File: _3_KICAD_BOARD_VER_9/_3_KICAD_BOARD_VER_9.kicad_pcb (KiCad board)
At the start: 4 copper layers, 85 x 87 mm, 60 parts, among them J1 HTEC8-160-01-X-DV-A-BL-X, J2 PH2-20-UA, J3 PH2-20-UA, J4 PH2-20-UA, J5 PH2-20-UA, J6 PH2-20-UA, U1 AZ1117H-3.3TRE1, U2 dsPIC33AK512MPS505T-I/PT, U3 DAC7564ICPW, U4 FM24W256G, Y1 ABMM-25.000MHZ-B2-T

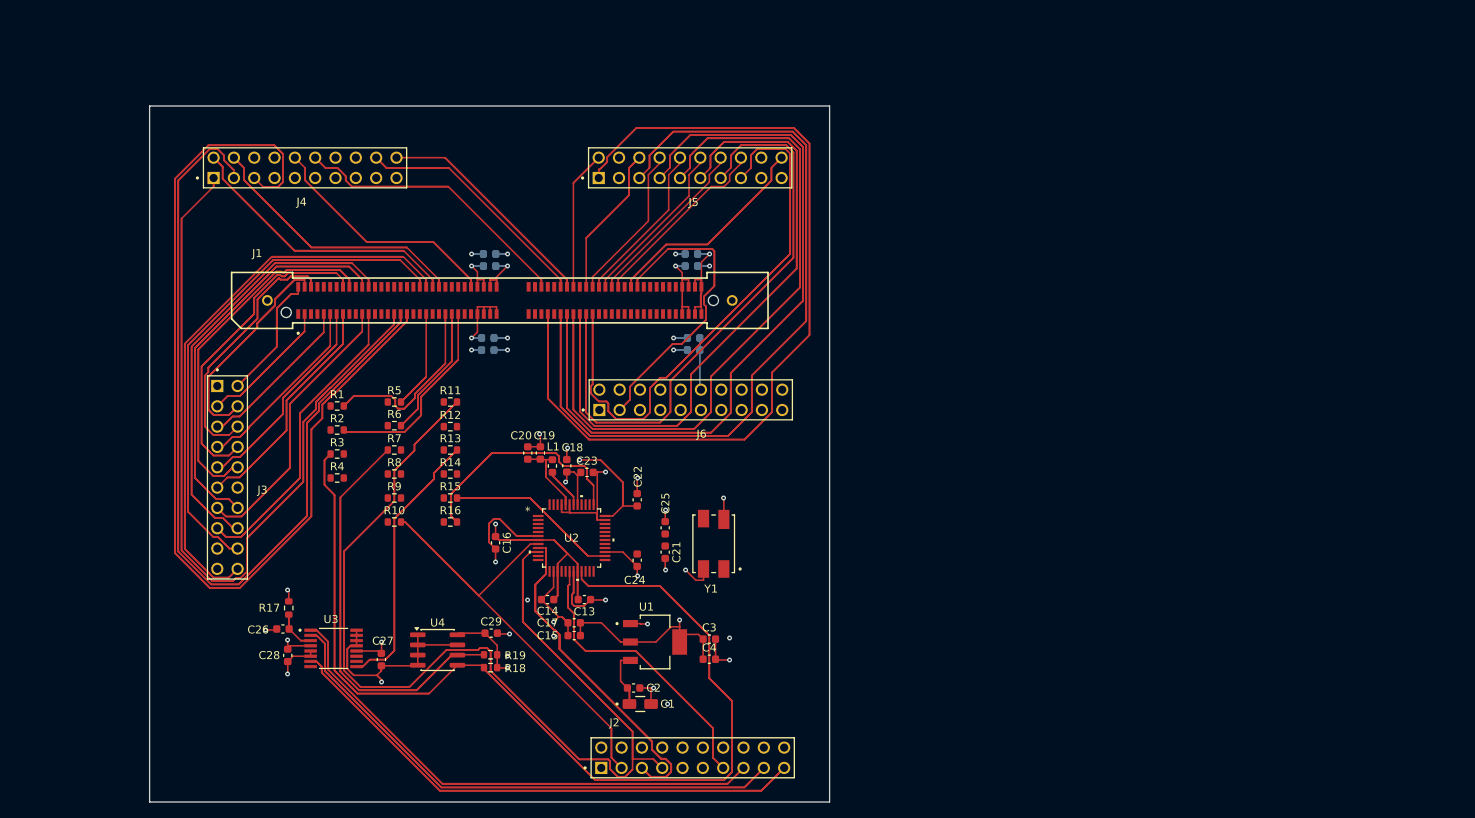
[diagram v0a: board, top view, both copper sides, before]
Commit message: feat : vdd, gnd, vin routing done
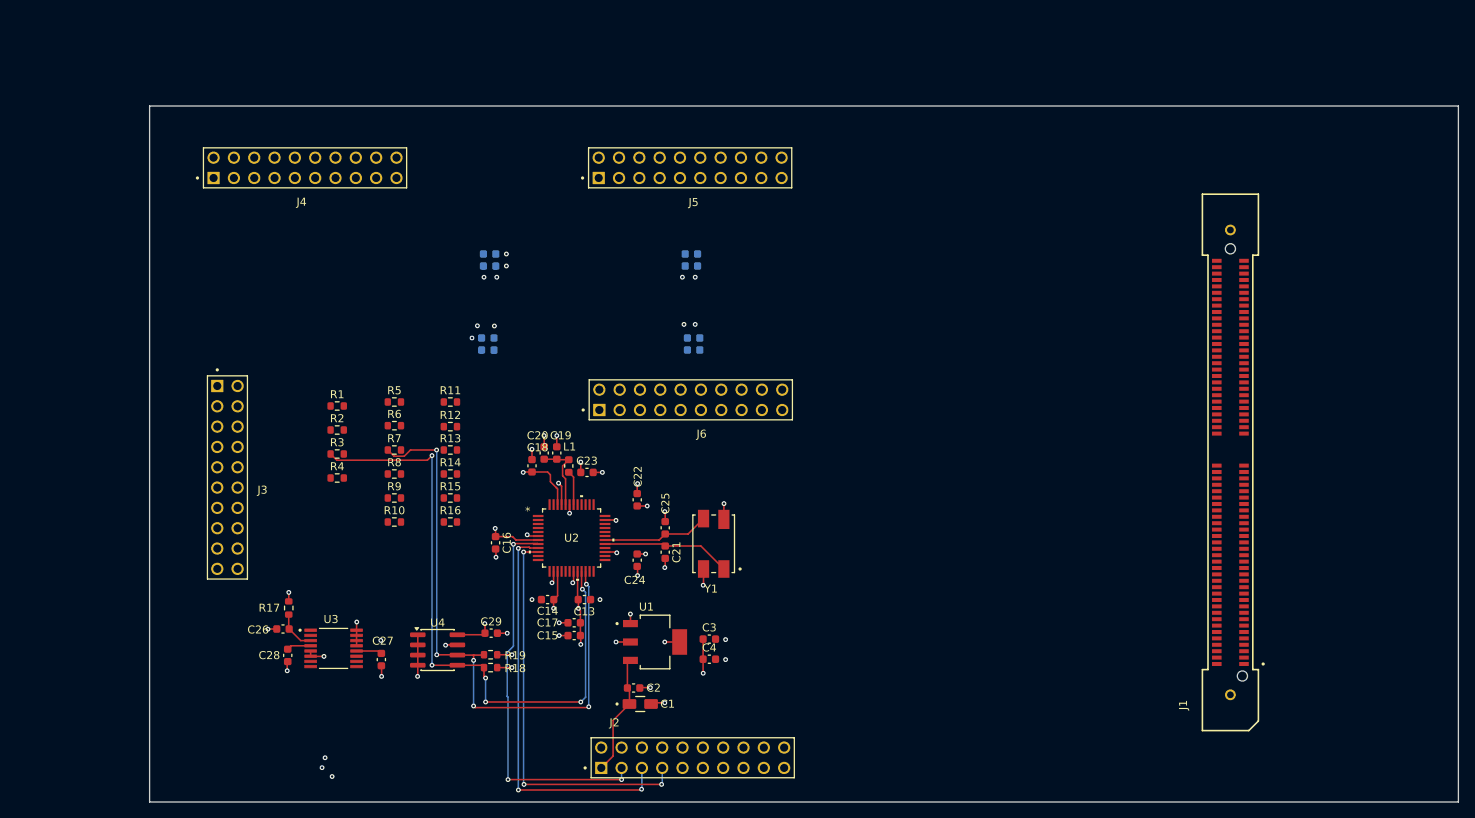
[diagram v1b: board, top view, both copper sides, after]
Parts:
- moved J1 93.5 mm to (220.1, 97.5), turned to 90 degrees
- moved C18 4.35 mm to (132.8, 98.0)
- moved C19 2.05 mm to (135.9, 96.4)
- moved L1 2.05 mm to (137.4, 98.0)
- moved C20 2.05 mm to (134.3, 96.4)
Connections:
- J1 pad 61: +3.3V -> GND
- J1 pad 63: +3.3V -> GND
- J2 pad 14: unconnected-(J2-Pad14) -> /DIM_SHEET/DEBUG_BUS.MCLR
- J2 pad 16: unconnected-(J2-Pad16) -> +3.3V
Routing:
- net /DIM_SHEET/DIM_BUS.IO24: track 244.8 -> 0.00 mm
- net /DIM_SHEET/DIM_BUS.IO22: track 216.8 -> 0.00 mm
- net /DIM_SHEET/DIM_BUS.IO40: track 215.6 -> 0.00 mm
- net /DIM_SHEET/DIM_BUS.IO44: track 196.8 -> 0.00 mm
- net /DIM_SHEET/ADC_BUS._A2: track 246.4 -> 50.3 mm, vias 0 -> 3
- net /DIM_SHEET/DIM_BUS.IO20: track 191.0 -> 0.00 mm
- net /DIM_SHEET/DIM_BUS.IO46: track 184.6 -> 0.00 mm
- net /DIM_SHEET/DIM_BUS.IO48: track 172.3 -> 0.00 mm
- net /DIM_SHEET/I2C_BUS.SDA: track 240.6 -> 79.1 mm, vias 0 -> 6
- net /DIM_SHEET/DIM_BUS.IO50: track 160.1 -> 0.00 mm
- net /DIM_SHEET/DIM_BUS.IO52: track 147.8 -> 0.00 mm
- net /DIM_SHEET/DIM_BUS.IO19: track 137.9 -> 0.00 mm
- net /DIM_SHEET/DIM_BUS.IO54: track 135.4 -> 0.00 mm
- net /SIGNAL_IO_SHEET/DAC_BUS._1: track 134.3 -> 0.00 mm, vias 0 -> 1
- net /SIGNAL_IO_SHEET/DAC_BUS._2: track 134.2 -> 0.00 mm, vias 0 -> 1
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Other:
- board size 85 x 87 mm -> 163.6 x 87 mm

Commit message: feat : dim only project done
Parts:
- removed C22, C23, C24, C26, C27, C28, C29: 100nF, Capacitor_SMD:C_0603_1608Metric
- removed C25: 18pF, Capacitor_SMD:C_0603_1608Metric
- removed J2, J3, J4, J5, J6: PH2-20-UA, PH2-20-UA:ADAM_PH2-20-UA
- removed R10, R11, R12, R13, R14, R15, R16, R4, R5, R6, R7, R8, R9: 0R, Resistor_SMD:R_0603_1608Metric
- removed R17: 100R, Resistor_SMD:R_0603_1608Metric
- removed R18, R19: 2.2K, Resistor_SMD:R_0603_1608Metric
- C10, C6: moved to F.Cu
- C11: value 100nF -> 10uF; moved to F.Cu
- C12, C5, C8: value 22uF -> 100nF; moved to F.Cu
- C13: value 100nF -> 18pF
- C15: value 47uF -> 100nF
- C17: value 1uF -> 18pF
- C19: value 10uF -> 100nF
- C21: value 18pF -> 100nF
- C7: value 100nF -> 47uF; moved to F.Cu
- C9: value 22uF -> 1uF; moved to F.Cu
- J1: value HTEC8-160-01-X-DV-A-BL-X -> PH2-20-UA; footprint HTEC8-160-01-X-DV-A-BL-X:SAMTEC_HTEC8-160-01-X-DV-A-BL-X -> PH2-20-UA:ADAM_PH2-20-UA
- R1: value 0R -> 100R
- R2, R3: value 0R -> 2.2K
- moved J1 124.5 mm to (102.5, 57.0), turned to 0 degrees
- moved C15 68.4 mm to (98.3, 63.5), turned to 0 degrees
- moved C2 65.1 mm to (126.3, 63.5)
- moved C17 63.2 mm to (98.3, 68.5), turned to 0 degrees
- moved C21 62.9 mm to (90.3, 87.3), turned to 0 degrees
- moved C13 62.7 mm to (94.3, 71.0)
- moved C1 62.6 mm to (117.6, 72.1)
- moved C9 62.4 mm to (90.3, 73.5)
- moved C11 61.2 mm to (94.3, 66.0)
- moved C3 60.8 mm to (126.3, 66.0)
- moved C4 60.8 mm to (126.3, 68.5)
- moved U1 60.8 mm to (119.5, 66.4)
- moved C12 60.2 mm to (94.3, 68.5)
- moved C10 59.0 mm to (94.3, 63.5)
- moved Y1 58.7 mm to (104.3, 79.0), turned to 0 degrees
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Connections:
- net /DIM_SHEET/SPI_BUS.MOSI renamed /MCU_48PIN_SHEET/SPI_BUS.MOSI
- net /DIM_SHEET/SPI_BUS.SCLK renamed /MCU_48PIN_SHEET/SPI_BUS.SCLK
- net /DIM_SHEET/SPI_BUS.SS renamed /MCU_48PIN_SHEET/SPI_BUS.SS
- C11 pad 1: +3.3V -> /MCU_48PIN_SHEET/VDD_CORE
- C12 pad 1: +3.3V -> /MCU_48PIN_SHEET/VDD_CORE
- C13 pad 1: +3.3V -> Net-(U2-OSCO/CLKO/RP33/IOMAF5/RC0)
- C17 pad 1: +3.3V -> Net-(U2-OSCI/CLKI/RP34/IOMAF6/RC1)
- C18 pad 1: +3.3V -> Net-(U3-VREFH/VREFOUT)
- C19 pad 1: /MCU_48PIN_SHEET/VDD_CORE -> +3.3V
- C20 pad 1: /MCU_48PIN_SHEET/VDD_CORE -> +3.3V
- C21 pad 1: Net-(U2-OSCO/CLKO/RP33/IOMAF5/RC0) -> +3.3V
- J1 pad 1: /DIM_SHEET/DIM_BUS.IO0 -> VIN
- J1 pad 10: unconnected-(J1-Pad10) -> /MCU_48PIN_SHEET/DEBUG_BUS.PGD
- J1 pad 11: /DIM_SHEET/DIM_BUS.IO6 -> /MCU_48PIN_SHEET/ADC_BUS._B1
- J1 pad 12: Net-(J1-Pad12) -> /MCU_48PIN_SHEET/DEBUG_BUS.PGC
- J1 pad 13: /DIM_SHEET/DIM_BUS.IO8 -> /MCU_48PIN_SHEET/ADC_BUS._B2
- J1 pad 14: Net-(J1-Pad14) -> /MCU_48PIN_SHEET/DEBUG_BUS.MCLR
- J1 pad 15: /DIM_SHEET/DIM_BUS.IO10 -> /SIGNAL_IO_SHEET/DAC_BUS._0
- J1 pad 16: /DIM_SHEET/DIM_BUS.IO7 -> +3.3V
- J1 pad 17: unconnected-(J1-Pad17) -> /SIGNAL_IO_SHEET/DAC_BUS._1
- J1 pad 18: /DIM_SHEET/DIM_BUS.IO9 -> /MCU_48PIN_SHEET/SYS_BUS.BAND_SELECT
- J1 pad 19: unconnected-(J1-Pad19) -> /SIGNAL_IO_SHEET/DAC_BUS._2
- J1 pad 2: /DIM_SHEET/DIM_BUS.IO1 -> +3.3V
- J1 pad 20: /DIM_SHEET/DIM_BUS.IO11 -> GND
- J1 pad 3: /DIM_SHEET/DIM_BUS.IO2 -> /MCU_48PIN_SHEET/ADC_BUS._A0
- J1 pad 4: /DIM_SHEET/DIM_BUS.IO3 -> GND
- J1 pad 5: Net-(J1-Pad5) -> /MCU_48PIN_SHEET/ADC_BUS._A1
- J1 pad 6: /DIM_SHEET/DIM_BUS.IO5 -> /MCU_48PIN_SHEET/UART_BUS.TX
- J1 pad 7: Net-(J1-Pad7) -> /MCU_48PIN_SHEET/ADC_BUS._A2
- J1 pad 8: unconnected-(J1-Pad8) -> /MCU_48PIN_SHEET/UART_BUS.RX
- J1 pad 9: /DIM_SHEET/DIM_BUS.IO4 -> /MCU_48PIN_SHEET/ADC_BUS._B0
- R1 pad 1: /DIM_SHEET/DEBUG_BUS.MCLR -> +3.3V
- R1 pad 2: Net-(J1-Pad47) -> Net-(U3-VREFH/VREFOUT)
- R2 pad 1: /DIM_SHEET/DEBUG_BUS.PGC -> /MCU_48PIN_SHEET/I2C_BUS.SDA
- R2 pad 2: Net-(J1-Pad51) -> +3.3V
- R3 pad 1: /DIM_SHEET/I2C_BUS.SDA -> /MCU_48PIN_SHEET/I2C_BUS.SCL
- R3 pad 2: Net-(J1-Pad5) -> +3.3V
- U2 pad 10: /DIM_SHEET/ADC_BUS._A2 -> /MCU_48PIN_SHEET/ADC_BUS._A2
- U2 pad 16: /DIM_SHEET/ADC_BUS._B0 -> /MCU_48PIN_SHEET/ADC_BUS._B0
- U2 pad 17: /DIM_SHEET/ADC_BUS._B1 -> /MCU_48PIN_SHEET/ADC_BUS._B1
- U2 pad 18: /DIM_SHEET/ADC_BUS._B2 -> /MCU_48PIN_SHEET/ADC_BUS._B2
- U2 pad 21: /DIM_SHEET/I2C_BUS.SDA -> /MCU_48PIN_SHEET/I2C_BUS.SDA
- U2 pad 22: /DIM_SHEET/I2C_BUS.SCL -> /MCU_48PIN_SHEET/I2C_BUS.SCL
- U2 pad 26: /DIM_SHEET/SPI_BUS.MISO -> /MCU_48PIN_SHEET/SPI_BUS.MISO
- U2 pad 31: /DIM_SHEET/DEBUG_BUS.PGC -> /MCU_48PIN_SHEET/DEBUG_BUS.PGC
- U2 pad 32: /DIM_SHEET/DEBUG_BUS.PGD -> /MCU_48PIN_SHEET/DEBUG_BUS.PGD
- U2 pad 38: /DIM_SHEET/SYS_BUS.BAND_SELECT -> /MCU_48PIN_SHEET/SYS_BUS.BAND_SELECT
- U2 pad 40: /DIM_SHEET/UART_BUS.TX -> /MCU_48PIN_SHEET/UART_BUS.TX
- U2 pad 47: /DIM_SHEET/UART_BUS.RX -> /MCU_48PIN_SHEET/UART_BUS.RX
- U2 pad 48: /DIM_SHEET/DEBUG_BUS.MCLR -> /MCU_48PIN_SHEET/DEBUG_BUS.MCLR
- U2 pad 8: /DIM_SHEET/ADC_BUS._A0 -> /MCU_48PIN_SHEET/ADC_BUS._A0
- U2 pad 9: /DIM_SHEET/ADC_BUS._A1 -> /MCU_48PIN_SHEET/ADC_BUS._A1
- U4 pad 5: /DIM_SHEET/I2C_BUS.SDA -> /MCU_48PIN_SHEET/I2C_BUS.SDA
- U4 pad 6: /DIM_SHEET/I2C_BUS.SCL -> /MCU_48PIN_SHEET/I2C_BUS.SCL
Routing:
- net /DIM_SHEET/I2C_BUS.SDA: track 79.1 -> 0.00 mm, vias 6 -> 0
- net /DIM_SHEET/I2C_BUS.SCL: track 76.3 -> 0.00 mm, vias 6 -> 0
- net +3.3V: track 55.9 -> 0.00 mm, vias 21 -> 0
- net /DIM_SHEET/ADC_BUS._A1: track 50.9 -> 0.00 mm, vias 3 -> 0
- net /DIM_SHEET/ADC_BUS._A2: track 50.3 -> 0.00 mm, vias 3 -> 0
- net GND: track 49.8 -> 0.00 mm, vias 41 -> 0
- net /DIM_SHEET/ADC_BUS._A0: track 48.6 -> 0.00 mm, vias 3 -> 0
- net Net-(U2-OSCO/CLKO/RP33/IOMAF5/RC0): track 16.2 -> 0.00 mm
- net VIN: track 15.2 -> 0.00 mm
- net Net-(U2-OSCI/CLKI/RP34/IOMAF6/RC1): track 13.4 -> 0.00 mm
- net /MCU_48PIN_SHEET/VDD_CORE: track 9.19 -> 0.00 mm
- net Net-(U3-VREFH/VREFOUT): track 5.11 -> 0.00 mm
- net /MCU_48PIN_SHEET/LX: track 4.29 -> 0.00 mm
- net /SIGNAL_IO_SHEET/DAC_BUS._2: vias 1 -> 0
- net /SIGNAL_IO_SHEET/DAC_BUS._1: vias 1 -> 0
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- removed copper zone on In2.Cu, net +3.3V
- removed copper zone on In1.Cu, net GND
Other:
- board size 163.6 x 87 mm -> 55 x 47 mm
- copper layers 4 -> 2

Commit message: feat : dim board base board 작업시작
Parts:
- moved C5 38.6 mm to (117.2, 91.1), turned to 180 degrees
- moved C13 38.3 mm to (129.2, 86.6), turned to -90 degrees
- moved C2 35.0 mm to (91.3, 63.8)
- moved C6 34.3 mm to (113.7, 91.1), turned to 180 degrees
- moved C17 34.1 mm to (129.2, 82.8), turned to 90 degrees
- moved C16 33.6 mm to (123.8, 88.0), turned to -90 degrees
- moved Y1 32.0 mm to (135.8, 85.1), turned to 180 degrees
- moved C14 30.6 mm to (123.8, 82.0), turned to -90 degrees
- moved C10 28.5 mm to (119.2, 77.2)
- moved C3 27.6 mm to (99.4, 72.5), turned to 90 degrees
- moved C1 27.5 mm to (92.2, 61.8)
- moved C19 27.3 mm to (135.8, 60.5), turned to -90 degrees
- moved U1 26.4 mm to (93.2, 69.5), turned to -90 degrees
- moved R1 26.3 mm to (120.2, 58.5)
- moved C4 24.7 mm to (101.9, 72.5), turned to 90 degrees
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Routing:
- net +3.3V: track 0.00 -> 186.1 mm, vias 0 -> 2
- net /MCU_48PIN_SHEET/ADC_BUS._A1: track 0.00 -> 49.2 mm, vias 0 -> 1
- net /MCU_48PIN_SHEET/DEBUG_BUS.PGC: track 0.00 -> 44.0 mm, vias 0 -> 1
- net /MCU_48PIN_SHEET/ADC_BUS._A0: track 0.00 -> 41.6 mm, vias 0 -> 1
- net /MCU_48PIN_SHEET/UART_BUS.TX: track 0.00 -> 40.3 mm, vias 0 -> 1
- net /MCU_48PIN_SHEET/DEBUG_BUS.PGD: track 0.00 -> 38.5 mm, vias 0 -> 2
- net /MCU_48PIN_SHEET/ADC_BUS._A2: track 0.00 -> 36.8 mm, vias 0 -> 1
- net /MCU_48PIN_SHEET/ADC_BUS._B0: track 0.00 -> 36.3 mm, vias 0 -> 1
- net /MCU_48PIN_SHEET/SPI_BUS.SCLK: track 0.00 -> 35.6 mm, vias 0 -> 2
- net /MCU_48PIN_SHEET/ADC_BUS._B1: track 0.00 -> 35.5 mm, vias 0 -> 1
- net /MCU_48PIN_SHEET/ADC_BUS._B2: track 0.00 -> 34.6 mm
- net /MCU_48PIN_SHEET/UART_BUS.RX: track 0.00 -> 32.1 mm, vias 0 -> 1
- net /MCU_48PIN_SHEET/I2C_BUS.SDA: track 0.00 -> 30.7 mm
- net /MCU_48PIN_SHEET/SYS_BUS.BAND_SELECT: track 0.00 -> 28.1 mm, vias 0 -> 1
- net /MCU_48PIN_SHEET/DEBUG_BUS.MCLR: track 0.00 -> 27.8 mm
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- added copper zone on B.Cu, net GND
- added copper zone on F.Cu, net GND

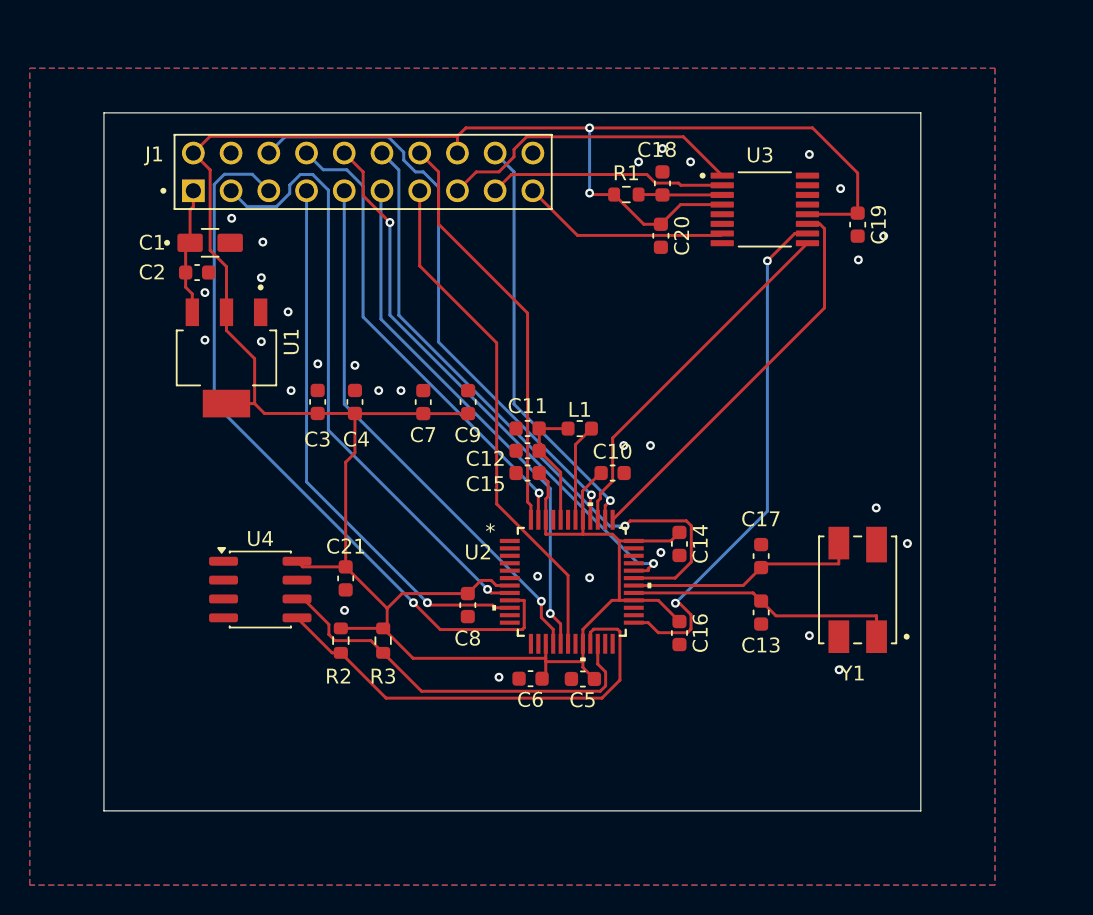
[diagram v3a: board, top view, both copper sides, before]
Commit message: feat : 회로도 수정, MCLR pull up 10K 추가, GND MCU쪽 floating 다수...
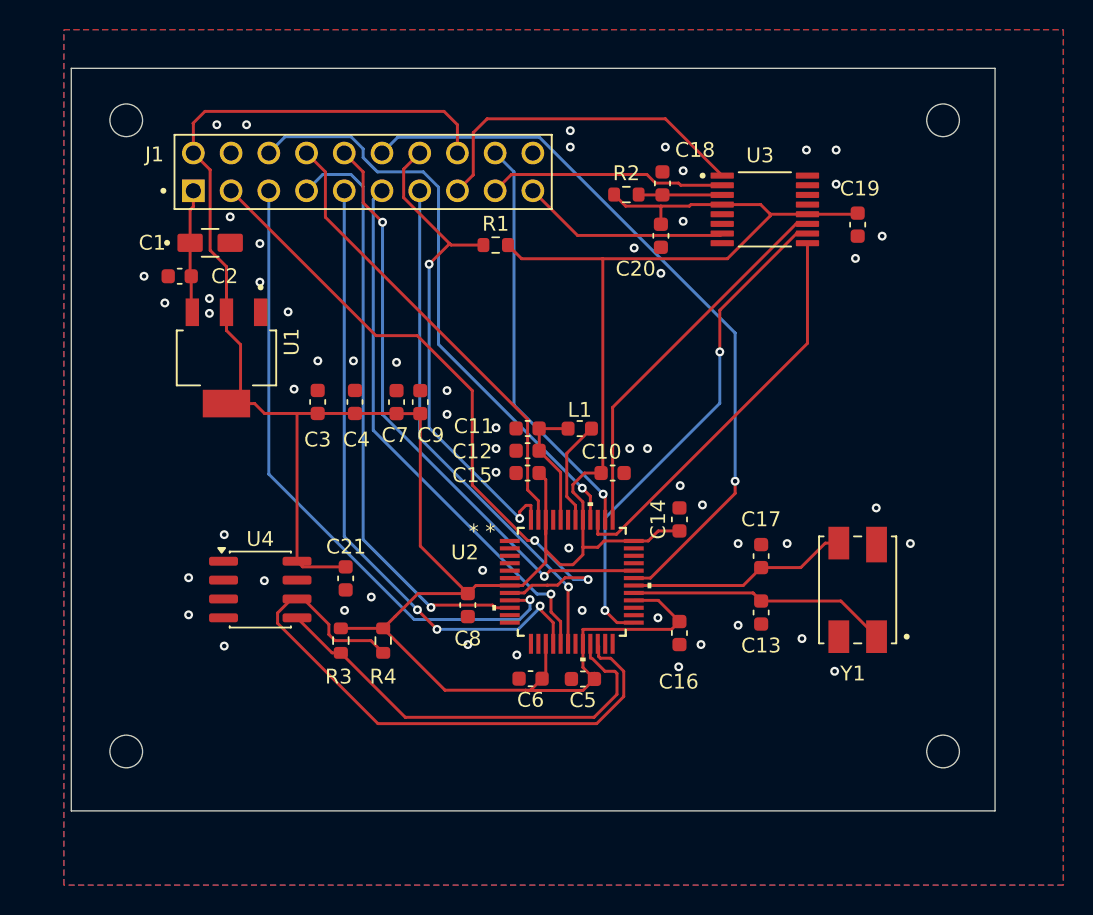
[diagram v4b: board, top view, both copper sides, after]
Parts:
- added R1: 10K, Resistor_SMD:R_0603_1608Metric, F.Cu at (111.4, 61.9)
- added REF**: MountingHole_2.2mm_M2, MountingHole:MountingHole_2.2mm_M2, F.Cu at (86.5, 53.5)
- added REF**: MountingHole_2.2mm_M2, MountingHole:MountingHole_2.2mm_M2, F.Cu at (141.5, 96.0)
- added REF**: MountingHole_2.2mm_M2, MountingHole:MountingHole_2.2mm_M2, F.Cu at (86.5, 96.0)
- added REF**: MountingHole_2.2mm_M2, MountingHole:MountingHole_2.2mm_M2, F.Cu at (141.5, 53.5)
- moved C9 3.22 mm to (106.3, 72.5)
- moved C7 1.80 mm to (104.7, 72.5)
- moved C14 1.65 mm to (123.8, 80.4), turned to 90 degrees
- moved C2 1.20 mm to (90.1, 64.0), turned to 180 degrees
- renumbered R1 to R2, R2 to R3, R3 to R4
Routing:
- net +3.3V: track 186.1 -> 207.7 mm, vias 2 -> 0
- net /MCU_48PIN_SHEET/I2C_BUS.SCL: track 27.0 -> 41.6 mm
- net /MCU_48PIN_SHEET/ADC_BUS._B0: track 36.3 -> 42.7 mm, vias 1 -> 3
- net /MCU_48PIN_SHEET/DEBUG_BUS.MCLR: track 27.8 -> 34.1 mm, vias 0 -> 2
- net /MCU_48PIN_SHEET/ADC_BUS._A1: track 49.2 -> 43.0 mm
- net /MCU_48PIN_SHEET/DEBUG_BUS.PGC: track 44.0 -> 49.7 mm
- net /MCU_48PIN_SHEET/ADC_BUS._A2: track 36.8 -> 40.3 mm
- net /MCU_48PIN_SHEET/ADC_BUS._A0: track 41.6 -> 44.4 mm, vias 1 -> 2
- net /MCU_48PIN_SHEET/SPI_BUS.SS: track 24.5 -> 27.2 mm
- net /SIGNAL_IO_SHEET/DAC_BUS._0: track 20.7 -> 23.1 mm
- net /MCU_48PIN_SHEET/SPI_BUS.SCLK: track 35.6 -> 33.7 mm
- net /MCU_48PIN_SHEET/DEBUG_BUS.PGD: track 38.5 -> 40.3 mm
- net /MCU_48PIN_SHEET/I2C_BUS.SDA: track 30.7 -> 29.4 mm
- net /MCU_48PIN_SHEET/SPI_BUS.MOSI: track 26.8 -> 25.8 mm
- net /MCU_48PIN_SHEET/ADC_BUS._B1: track 35.5 -> 36.5 mm
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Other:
- board size 55 x 47 mm -> 62.2 x 50 mm
